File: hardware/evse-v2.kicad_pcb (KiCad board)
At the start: 4 copper layers, 74 x 115 mm, 138 parts, among them J101 Boot, P101 CON-SENSOR2, P102 Relay, P103 L'+PE, P104 L'+PE, P105 CP/PP/PE, P106 Power, P107 Motor, P108 Switch_LED, P109 Enable, P110 MODBUS, P111 Debug, P112 DC-Protect, P113 GP, Q101 2N7002P, Q102 SI2305CDS-T1-GE3, Q103 2N7002P, Q104 2N7002P, Q105 SSM3J355R,LF, SW101 OS103011MS8QP1, SW102 OS103011MS8QP1, U101 XMC1404, U102 PEM1-S12-D12-S, U103 DMMT5401, U105 OPA171AIDBV, U106 A5950GLP, U108 AQH3213AX, U109 HCPL2731, U110 TPS70933DBVR, U111 IRM02-12, U112 WPMDL110, U113 SP3491, X101 16MHz

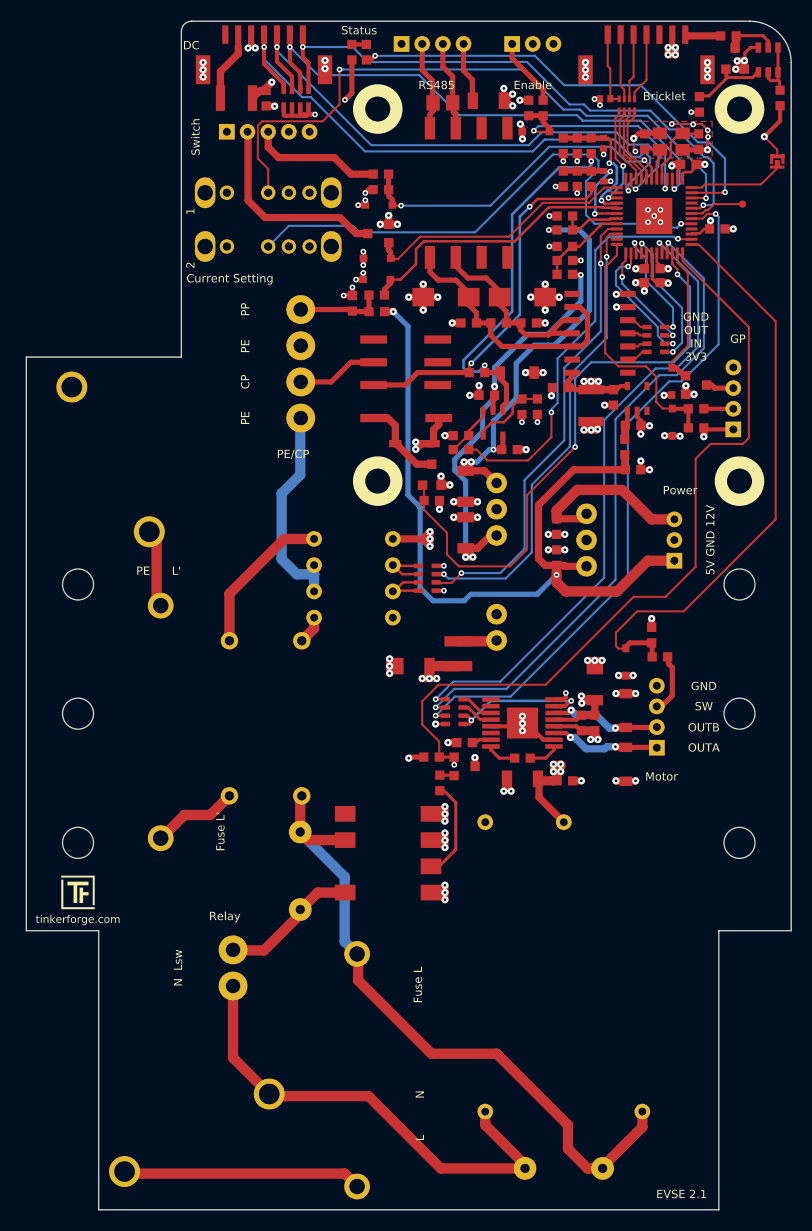
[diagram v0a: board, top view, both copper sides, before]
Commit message: fix connector positions, make pcb 1mm shorter, add fiducials
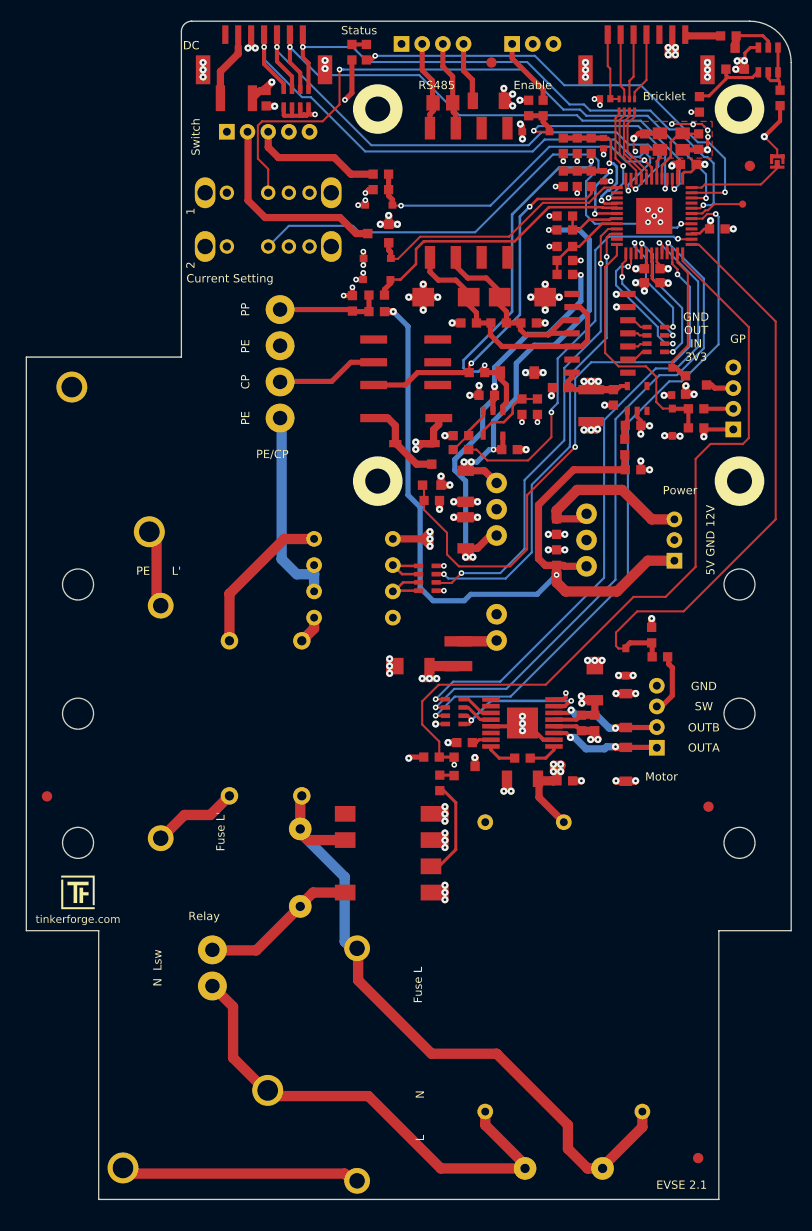
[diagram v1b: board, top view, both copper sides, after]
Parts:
- added Fiducial_Mark: VAL**, kicad-libraries:Fiducial_Mark, F.Cu at (143.3, 127.5)
- added Fiducial_Mark: VAL**, kicad-libraries:Fiducial_Mark, F.Cu at (122.3, 55.5)
- added Fiducial_Mark: VAL**, kicad-libraries:Fiducial_Mark, F.Cu at (147.3, 65.5)
- added Fiducial_Mark: VAL**, kicad-libraries:Fiducial_Mark, F.Cu at (79.3, 126.5)
- added Fiducial_Mark: VAL**, kicad-libraries:Fiducial_Mark, F.Cu at (142.3, 161.6)
- moved P102 2.00 mm to (95.3, 143.2)
- moved P105 2.00 mm to (101.9, 84.7)
- moved F101 0.55 mm to (109.3, 152.5)
- moved P103 0.38 mm to (100.7, 155.0)
- moved R113 0.30 mm to (103.8, 133.4)
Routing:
- net CPOUT2: track 6.79 -> 9.87 mm
- net Net-(P105-Pad4): track 7.23 -> 10.2 mm
- net Net-(P102-Pad2): track 13.4 -> 15.4 mm
- net N: track 46.8 -> 47.6 mm
- net GND: track 177.5 -> 176.8 mm
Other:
- board size 74 x 115 mm -> 74 x 114 mm

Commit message: ordered prototype
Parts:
- moved U103 12.4 mm to (147.8, 67.6), turned to 270 degrees
- moved R140 12.2 mm to (147.6, 70.8)
- moved L103 11.8 mm to (150.1, 63.8), turned to 90 degrees
- moved Fiducial_Mark 10.5 mm to (147.3, 55.0)
- moved Q105 9.46 mm to (147.9, 64.4), turned to 90 degrees
- moved J101 5.95 mm to (149.9, 71.1), turned to 90 degrees
- moved R133 5.54 mm to (145.2, 64.4)
- moved D114 1.90 mm to (139.8, 84.5)
- moved Q104 1.90 mm to (142.2, 84.8)
- moved R139 1.90 mm to (142.2, 89.0)
- moved D113 1.90 mm to (139.8, 88.5)
- moved P113 1.90 mm to (145.8, 86.2)
- moved R123 1.90 mm to (142.2, 87.2)
- moved RP102 1.73 mm to (138.6, 80.7)
- moved A101 1.70 mm to (146.3, 94.3)
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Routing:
- net Net-(L103-Pad2): track 3.40 -> 20.9 mm
- net 5V: track 265.6 -> 269.7 mm
- net MOTOR_ENABLE: track 63.1 -> 65.9 mm
- net Net-(RP102-Pad8): track 2.26 -> 4.93 mm
- net GND: track 176.8 -> 174.2 mm
- net ~MOTOR_FAULT: track 67.5 -> 70.0 mm
- net MOTOR_PHASE: track 62.1 -> 64.6 mm
- net Net-(Q105-PadG): track 7.67 -> 5.34 mm
- net VCC: track 223.1 -> 225.1 mm
- net CP-DISCONNECT: track 57.2 -> 55.2 mm
- net 485-R: track 14.3 -> 12.5 mm
- net Net-(D112-Pad1): track 8.57 -> 10.4 mm
- net GP-IN: track 24.6 -> 22.8 mm
- net GP-OUT: track 13.8 -> 12.0 mm
- net Net-(RP102-Pad7): track 2.04 -> 3.68 mm
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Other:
- board text added: "3V3"
- board text added: "IN"
- board text added: "OUT"
- board text removed: "GND OUT IN 3V3"
- board text removed: "TBD Pulldown"

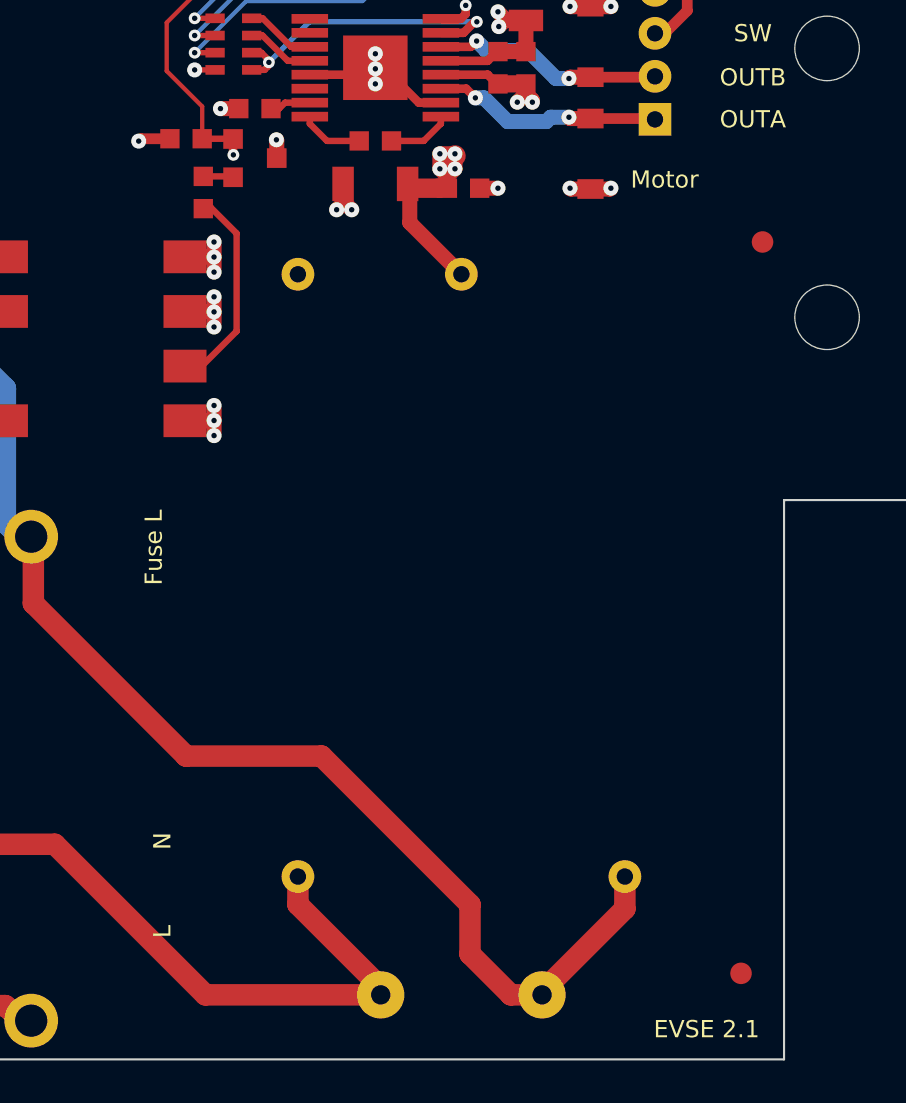
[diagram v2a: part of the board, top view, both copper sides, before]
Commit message: version 2.2: bugfix pullup relay
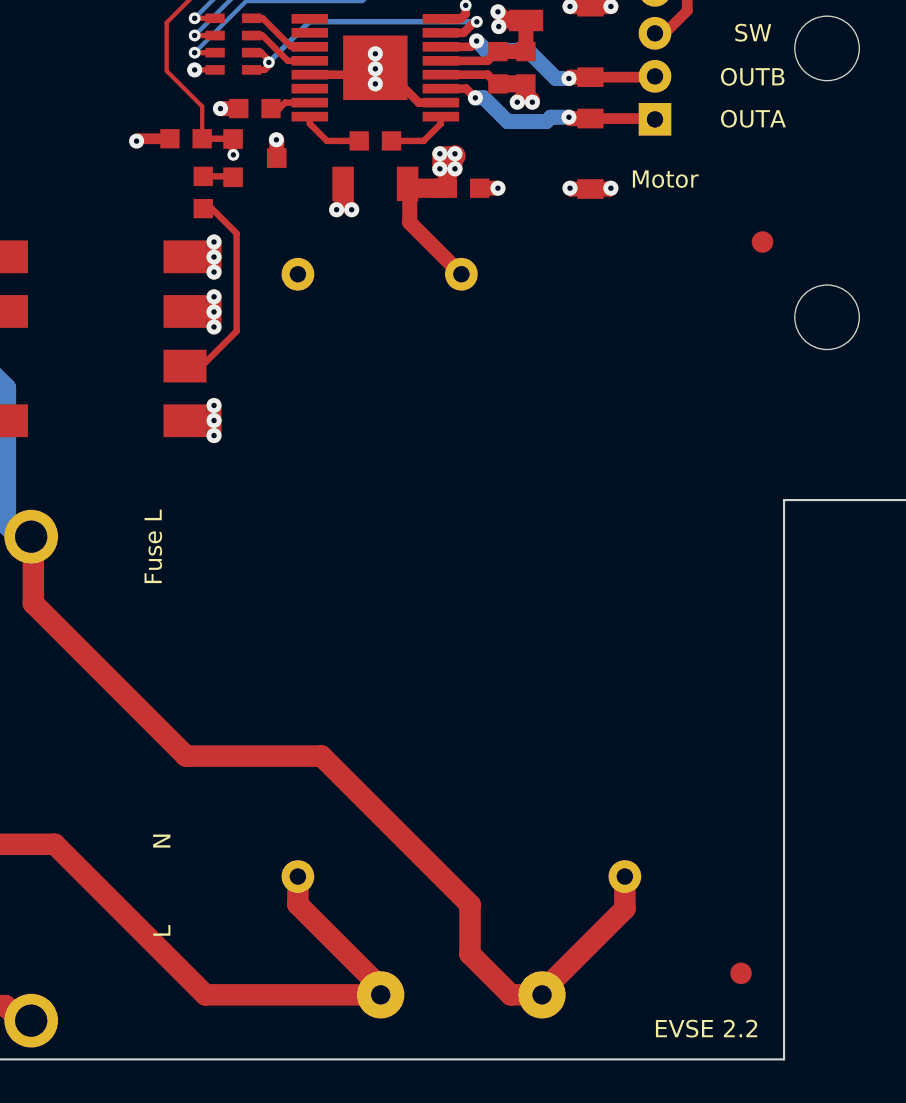
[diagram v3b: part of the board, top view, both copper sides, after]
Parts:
- turned R115 to 180 degrees
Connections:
- R115 pad 1: GND -> RELAY
- R115 pad 2: RELAY -> 3V3
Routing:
- net 3V3: track 103.3 -> 104.9 mm, vias 27 -> 28
- net GND: track 174.2 -> 172.7 mm, vias 133 -> 132
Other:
- board text added: "EVSE 2.2"
- board text removed: "EVSE 2.1"

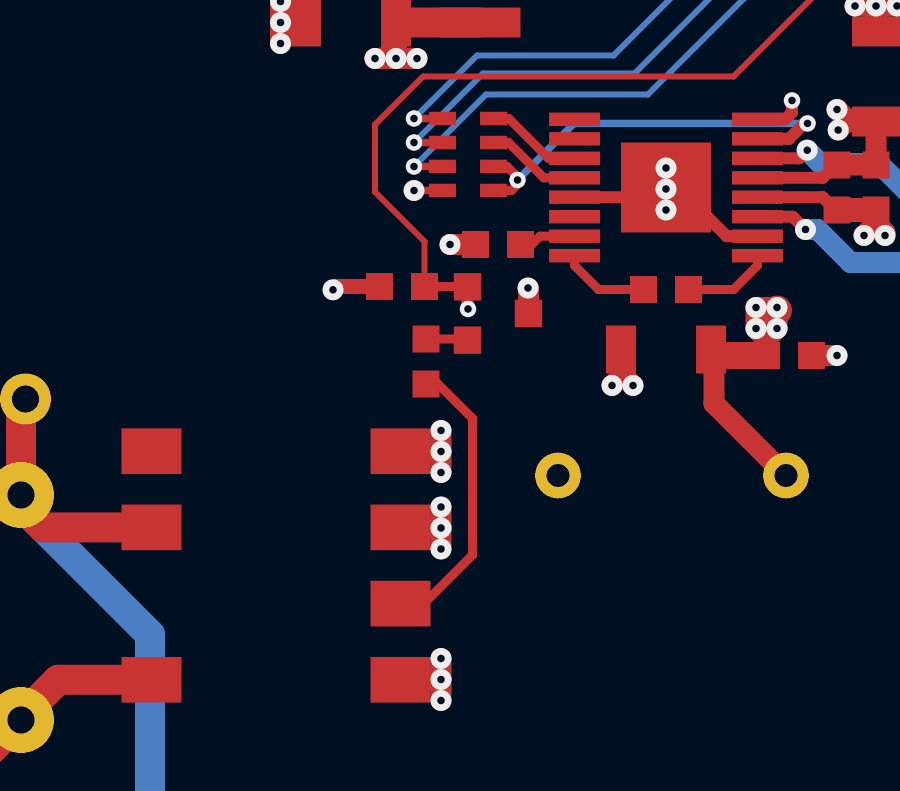
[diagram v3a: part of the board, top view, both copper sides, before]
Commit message: bugfix p ch mosfet orientation relay
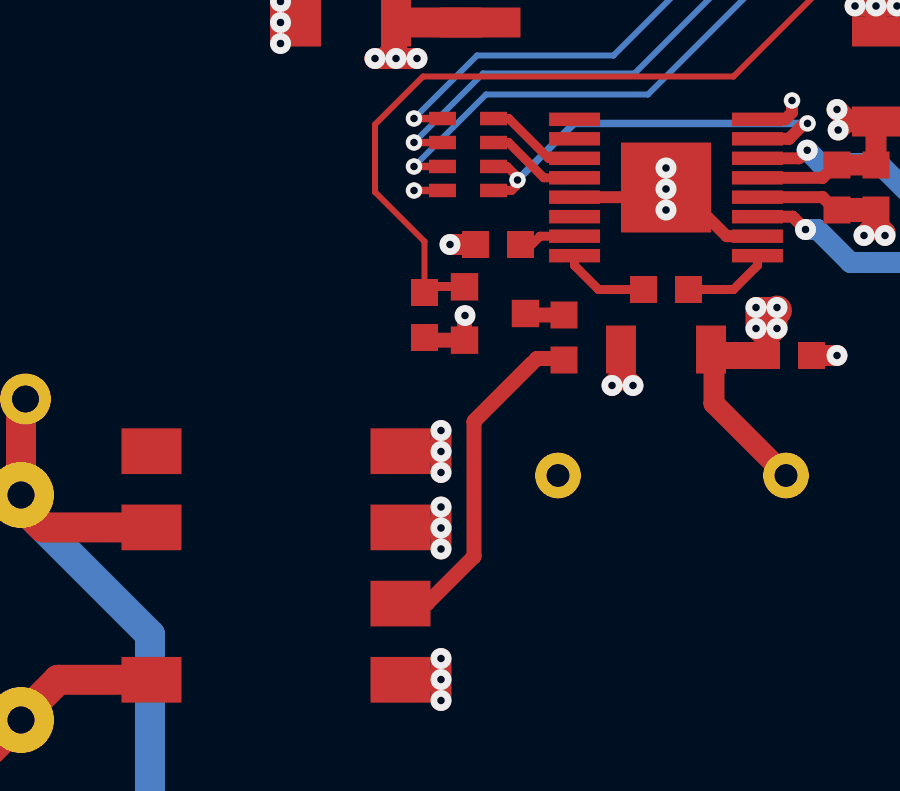
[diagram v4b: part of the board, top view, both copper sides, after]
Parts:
- moved R114 4.67 mm to (122.0, 124.5)
- moved R115 1.21 mm to (117.3, 123.7), turned to 270 degrees
- moved Q102 0.10 mm to (119.7, 123.7)
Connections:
- Q102 pad D: 3V3 -> Net-(Q102-PadD)
- Q102 pad S: Net-(Q102-PadS) -> 3V3
- R114 pad 1: Net-(Q102-PadS) -> Net-(Q102-PadD)
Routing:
- net 3V3: track 104.9 -> 84.7 mm, vias 28 -> 27
- net Net-(R114-Pad2): track 9.67 -> 22.9 mm
- net Net-(Q102-PadS): track 1.37 -> 0.00 mm
- net Net-(Q102-PadD): track 0.00 -> 1.22 mm
- net RELAY: track 76.6 -> 75.8 mm, vias 1 -> 0

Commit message: ordered prototype
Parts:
- moved P101 0.15 mm to (137.3, 57.5)
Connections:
- RP105 pad 2: AC1 -> AC2
- RP105 pad 3: AC2 -> AC1
- U101 pad 10: AC1 -> AC2
- U101 pad 9: AC2 -> AC1

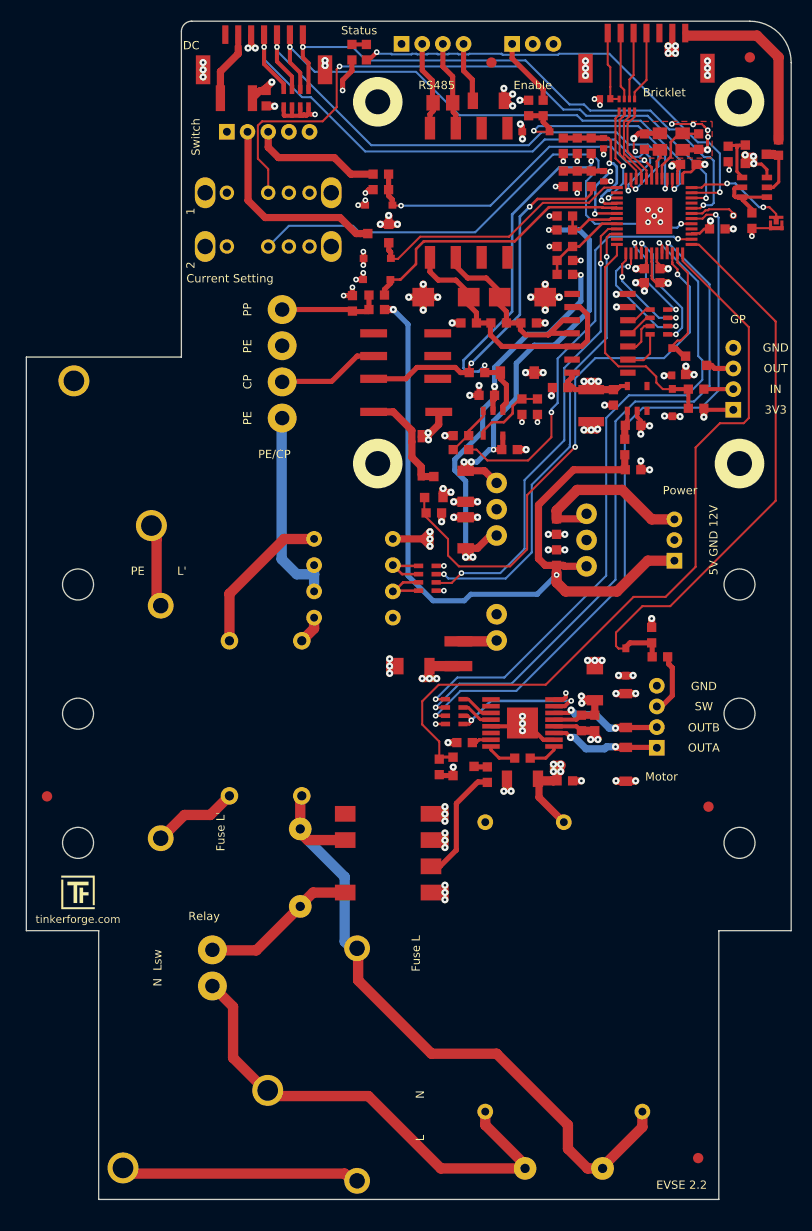
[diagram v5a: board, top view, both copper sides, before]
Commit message: start evse 2.3
 * change 120 ohm footprint to 0805
 * move esd diode
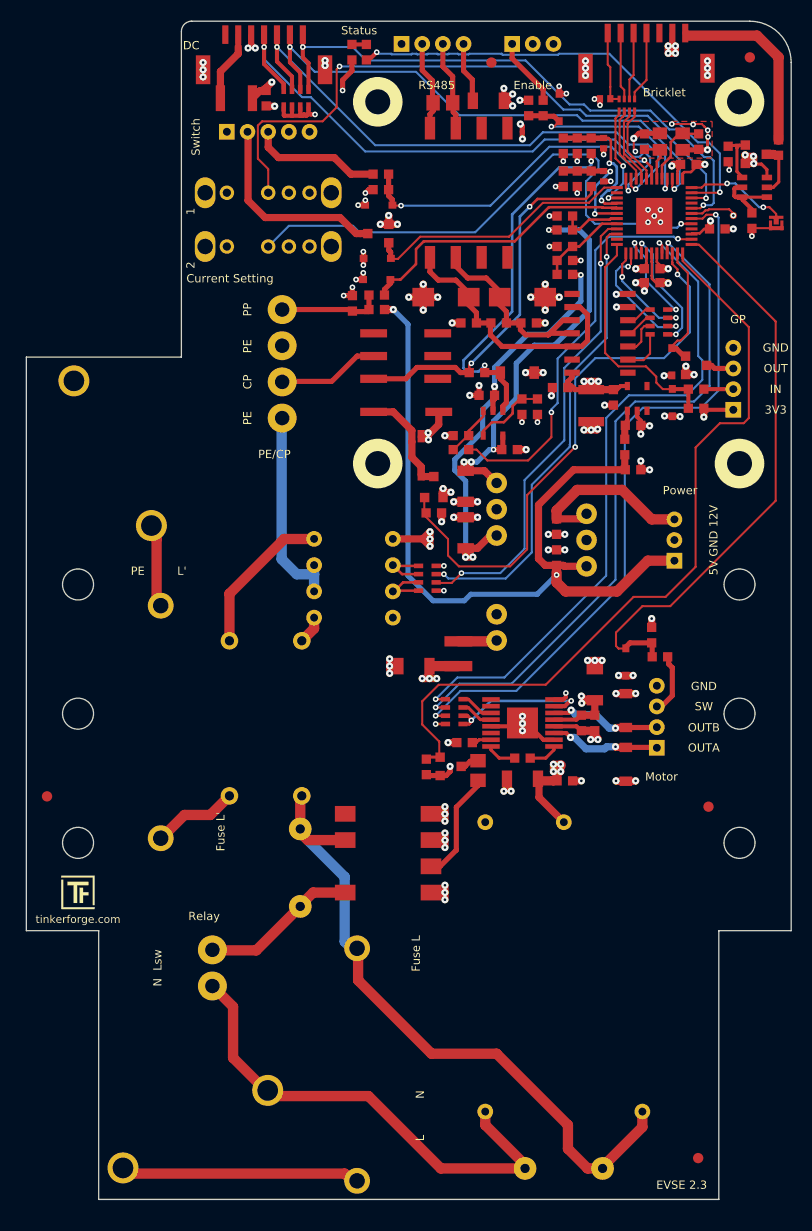
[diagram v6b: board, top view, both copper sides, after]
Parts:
- R114: footprint kicad-libraries:R0603F -> kicad-libraries:R0805E
- moved D102 3.25 mm to (128.9, 59.9), turned to 90 degrees
- moved Q102 1.25 mm to (118.4, 123.7)
- moved R115 1.25 mm to (116.0, 123.7)
- moved R114 0.98 mm to (121.0, 124.0)
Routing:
- net ENABLE: track 23.2 -> 20.7 mm
- net Net-(R114-Pad2): track 22.9 -> 20.9 mm
- net GND: track 172.7 -> 174.1 mm, vias 132 -> 134
- net 3V3: track 84.7 -> 85.5 mm
- net Net-(Q102-PadD): track 1.22 -> 1.91 mm
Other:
- board text added: "EVSE 2.3"
- board text removed: "74mm = 4TE"
- board text removed: "EVSE 2.2"

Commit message: more changes
 change relay connector
 move connectors
 integrate inline diodes
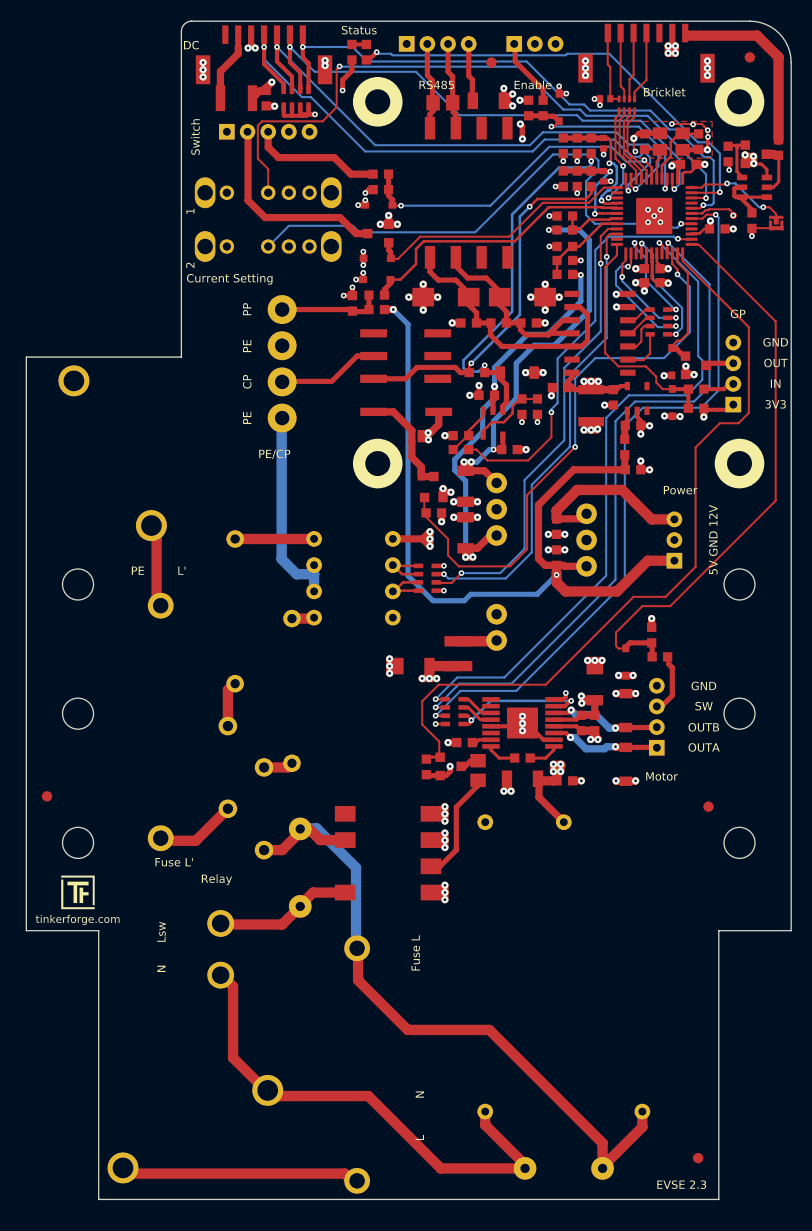
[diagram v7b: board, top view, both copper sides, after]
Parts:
- added D115: 1N4007, kicad-libraries:DO-41, F.Cu at (96.8, 123.8)
- added D116: 1N4007, kicad-libraries:DO-41, F.Cu at (100.3, 127.8)
- P102: footprint kicad-libraries:OQ_2P_Vertical -> kicad-libraries:OQ_2P_5mm_Vertical
- moved R118 10.4 mm to (97.5, 108.7)
- moved R116 2.82 mm to (103.0, 116.3)
- moved P102 1.97 mm to (96.2, 141.3)
- moved P110 0.50 mm to (117.2, 53.8)
- moved P113 0.50 mm to (145.8, 85.7)
- moved P109 0.20 mm to (126.5, 53.8)
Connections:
- F102 pad 2: Net-(F102-Pad2) -> Net-(D115-Pad1)
- R116 pad 1: L -> Net-(D116-Pad2)
- R118 pad 1: Net-(F102-Pad2) -> Net-(D115-Pad2)
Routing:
- net Net-(F102-Pad2): track 8.37 -> 0.00 mm
- net Net-(D115-Pad1): track 0.00 -> 7.87 mm
- net Net-(R118-Pad2): track 14.9 -> 7.60 mm
- net Net-(D115-Pad2): track 0.00 -> 4.45 mm
- net Net-(D116-Pad2): track 0.00 -> 2.87 mm
- net L: track 64.7 -> 67.0 mm
- net Net-(P102-Pad2): track 15.4 -> 13.7 mm
- net Net-(R116-Pad2): track 2.98 -> 2.10 mm
- net N: track 47.6 -> 48.4 mm
